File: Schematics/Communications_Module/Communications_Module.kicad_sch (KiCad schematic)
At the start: 72 parts, among them J1 USB_B_Micro, J2 SWD_01x04_Pin, J3 Stack Male Edge Connector, Q1 AO3400A, SW1 SW_STM_RESET, SW2 SW_STM_BOOT_MODE, U1 RFM95W-915S2, U2 W25Q128JVS, U3 AMS1117-3.3, U4 LM66100DCKR, U5 LM66100DCKR, U6 LM66100DCKR, U7 STM32F103CBT6, U8 ACS70331EOLC, U9 ISO1042BDWVR, Y1 X322516MMB4SI

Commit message: Power routed?
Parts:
- renumbered C6 to C5, C5 to C6, C2 to C7
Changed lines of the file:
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@@
     (title "QRET 23-24 SRAD Communications Module")
     (date "2024-03-09")
-    (rev "V0.3.0")
+    (rev "V0.3.1")
     (company "Queen's Rocket Engineering Team")
     (comment 1 "Contributors: Oak Campbell, Kennan Bays")
@@
   (symbol (lib_id "power:GND") (at 403.225 66.04 90) (unit 1)
     (in_bom yes) (on_board yes) (dnp no) (fields_autoplaced)
-    (property "Reference" "#PWR051" (at 409.575 66.04 0)
+    (property "Reference" "#PWR052" (at 409.575 66.04 0)
       (effects (font (size 1.27 1.27)) hide)
     )
@@
       (project "Communications_Module"
         (path "/ace06731-9b48-45c3-868d-c65fed1a8f9b"
-          (reference "#PWR051") (unit 1)
+          (reference "#PWR052") (unit 1)
         )
       )
@@
   (symbol (lib_id "power:GND") (at 403.86 46.99 0) (unit 1)
     (in_bom yes) (on_board yes) (dnp no)
-    (property "Reference" "#PWR053" (at 403.86 53.34 0)
+    (property "Reference" "#PWR054" (at 403.86 53.34 0)
       (effects (font (size 1.27 1.27)) hide)
     )
@@
       (project "Communications_Module"
         (path "/ace06731-9b48-45c3-868d-c65fed1a8f9b"
-          (reference "#PWR053") (unit 1)
+          (reference "#PWR054") (unit 1)
         )
       )
@@
   (symbol (lib_id "power:+3.3V") (at 403.86 31.75 0) (unit 1)
     (in_bom yes) (on_board yes) (dnp no)
-    (property "Reference" "#PWR052" (at 403.86 35.56 0)
+    (property "Reference" "#PWR053" (at 403.86 35.56 0)
       (effects (font (size 1.27 1.27)) hide)
     )
@@
       (project "Communications_Module"
         (path "/ace06731-9b48-45c3-868d-c65fed1a8f9b"
-          (reference "#PWR052") (unit 1)
+          (reference "#PWR053") (unit 1)
         )
       )
@@
   (symbol (lib_id "power:GND") (at 400.05 198.12 180) (unit 1)
     (in_bom yes) (on_board yes) (dnp no) (fields_autoplaced)
-    (property "Reference" "#PWR050" (at 400.05 191.77 0)
+    (property "Reference" "#PWR051" (at 400.05 191.77 0)
       (effects (font (size 1.27 1.27)) hide)
     )
@@
       (project "Communications_Module"
         (path "/ace06731-9b48-45c3-868d-c65fed1a8f9b"
-          (reference "#PWR050") (unit 1)
+          (reference "#PWR051") (unit 1)
         )
       )
@@
   (symbol (lib_id "Device:C") (at 92.71 253.365 0) (unit 1)
     (in_bom yes) (on_board yes) (dnp no)
-    (property "Reference" "C5" (at 86.36 252.095 0)
+    (property "Reference" "C6" (at 86.36 252.095 0)
       (effects (font (size 1.27 1.27)) (justify left))
     )
@@
       (project "Communications_Module"
         (path "/ace06731-9b48-45c3-868d-c65fed1a8f9b"
-          (reference "C5") (unit 1)
+          (reference "C6") (unit 1)
         )
       )
@@
   (symbol (lib_id "power:GND") (at 395.605 173.99 0) (unit 1)
     (in_bom yes) (on_board yes) (dnp no) (fields_autoplaced)
-    (property "Reference" "#PWR056" (at 395.605 180.34 0)
+    (property "Reference" "#PWR049" (at 395.605 180.34 0)
       (effects (font (size 1.27 1.27)) hide)
     )
@@
       (project "Communications_Module"
         (path "/ace06731-9b48-45c3-868d-c65fed1a8f9b"
-          (reference "#PWR056") (unit 1)
+          (reference "#PWR049") (unit 1)
         )
       )
@@
   (symbol (lib_id "Device:C_Polarized") (at 175.26 235.585 0) (unit 1)
     (in_bom yes) (on_board yes) (dnp no)
-    (property "Reference" "C2" (at 168.275 236.22 0)
+    (property "Reference" "C7" (at 168.275 236.22 0)
       (effects (font (size 1.27 1.27)) (justify left))
     )
@@
       (project "Communications_Module"
         (path "/ace06731-9b48-45c3-868d-c65fed1a8f9b"
-          (reference "C2") (unit 1)
+          (reference "C7") (unit 1)
         )
       )
@@
   (symbol (lib_id "power:+5V") (at 388.62 149.86 270) (unit 1)
     (in_bom yes) (on_board yes) (dnp no)
-    (property "Reference" "#PWR049" (at 384.81 149.86 0)
+    (property "Reference" "#PWR047" (at 384.81 149.86 0)
       (effects (font (size 1.27 1.27)) hide)
     )
@@
       (project "Communications_Module"
         (path "/ace06731-9b48-45c3-868d-c65fed1a8f9b"
-          (reference "#PWR049") (unit 1)
+          (reference "#PWR047") (unit 1)
         )
       )
@@
   (symbol (lib_id "power:GND") (at 397.51 220.98 0) (unit 1)
     (in_bom yes) (on_board yes) (dnp no) (fields_autoplaced)
-    (property "Reference" "#PWR047" (at 397.51 227.33 0)
+    (property "Reference" "#PWR050" (at 397.51 227.33 0)
       (effects (font (size 1.27 1.27)) hide)
     )
@@
       (project "Communications_Module"
         (path "/ace06731-9b48-45c3-868d-c65fed1a8f9b"
-          (reference "#PWR047") (unit 1)
+          (reference "#PWR050") (unit 1)
         )
       )
@@
   (symbol (lib_id "power:GND") (at 92.71 257.175 0) (unit 1)
     (in_bom yes) (on_board yes) (dnp no) (fields_autoplaced)
-    (property "Reference" "#PWR015" (at 92.71 263.525 0)
+    (property "Reference" "#PWR016" (at 92.71 263.525 0)
       (effects (font (size 1.27 1.27)) hide)
     )
@@
       (project "Communications_Module"
         (path "/ace06731-9b48-45c3-868d-c65fed1a8f9b"
-          (reference "#PWR015") (unit 1)
+          (reference "#PWR016") (unit 1)
         )
       )
@@
   (symbol (lib_id "power:GND") (at 92.71 238.125 0) (unit 1)
     (in_bom yes) (on_board yes) (dnp no) (fields_autoplaced)
-    (property "Reference" "#PWR016" (at 92.71 244.475 0)
+    (property "Reference" "#PWR015" (at 92.71 244.475 0)
       (effects (font (size 1.27 1.27)) hide)
     )
@@
       (project "Communications_Module"
         (path "/ace06731-9b48-45c3-868d-c65fed1a8f9b"
-          (reference "#PWR016") (unit 1)
+          (reference "#PWR015") (unit 1)
         )
       )
@@
   (symbol (lib_id "power:+5V") (at 408.94 205.74 270) (unit 1)
     (in_bom yes) (on_board yes) (dnp no)
-    (property "Reference" "#PWR054" (at 405.13 205.74 0)
+    (property "Reference" "#PWR055" (at 405.13 205.74 0)
       (effects (font (size 1.27 1.27)) hide)
     )
@@
       (project "Communications_Module"
         (path "/ace06731-9b48-45c3-868d-c65fed1a8f9b"
-          (reference "#PWR054") (unit 1)
+          (reference "#PWR055") (unit 1)
         )
       )
@@
   (symbol (lib_id "Device:C") (at 92.71 234.315 0) (unit 1)
     (in_bom yes) (on_board yes) (dnp no)
-    (property "Reference" "C6" (at 86.36 233.045 0)
+    (property "Reference" "C5" (at 86.36 233.045 0)
       (effects (font (size 1.27 1.27)) (justify left))
     )
@@
       (project "Communications_Module"
         (path "/ace06731-9b48-45c3-868d-c65fed1a8f9b"
-          (reference "C6") (unit 1)
+          (reference "C5") (unit 1)
         )
       )

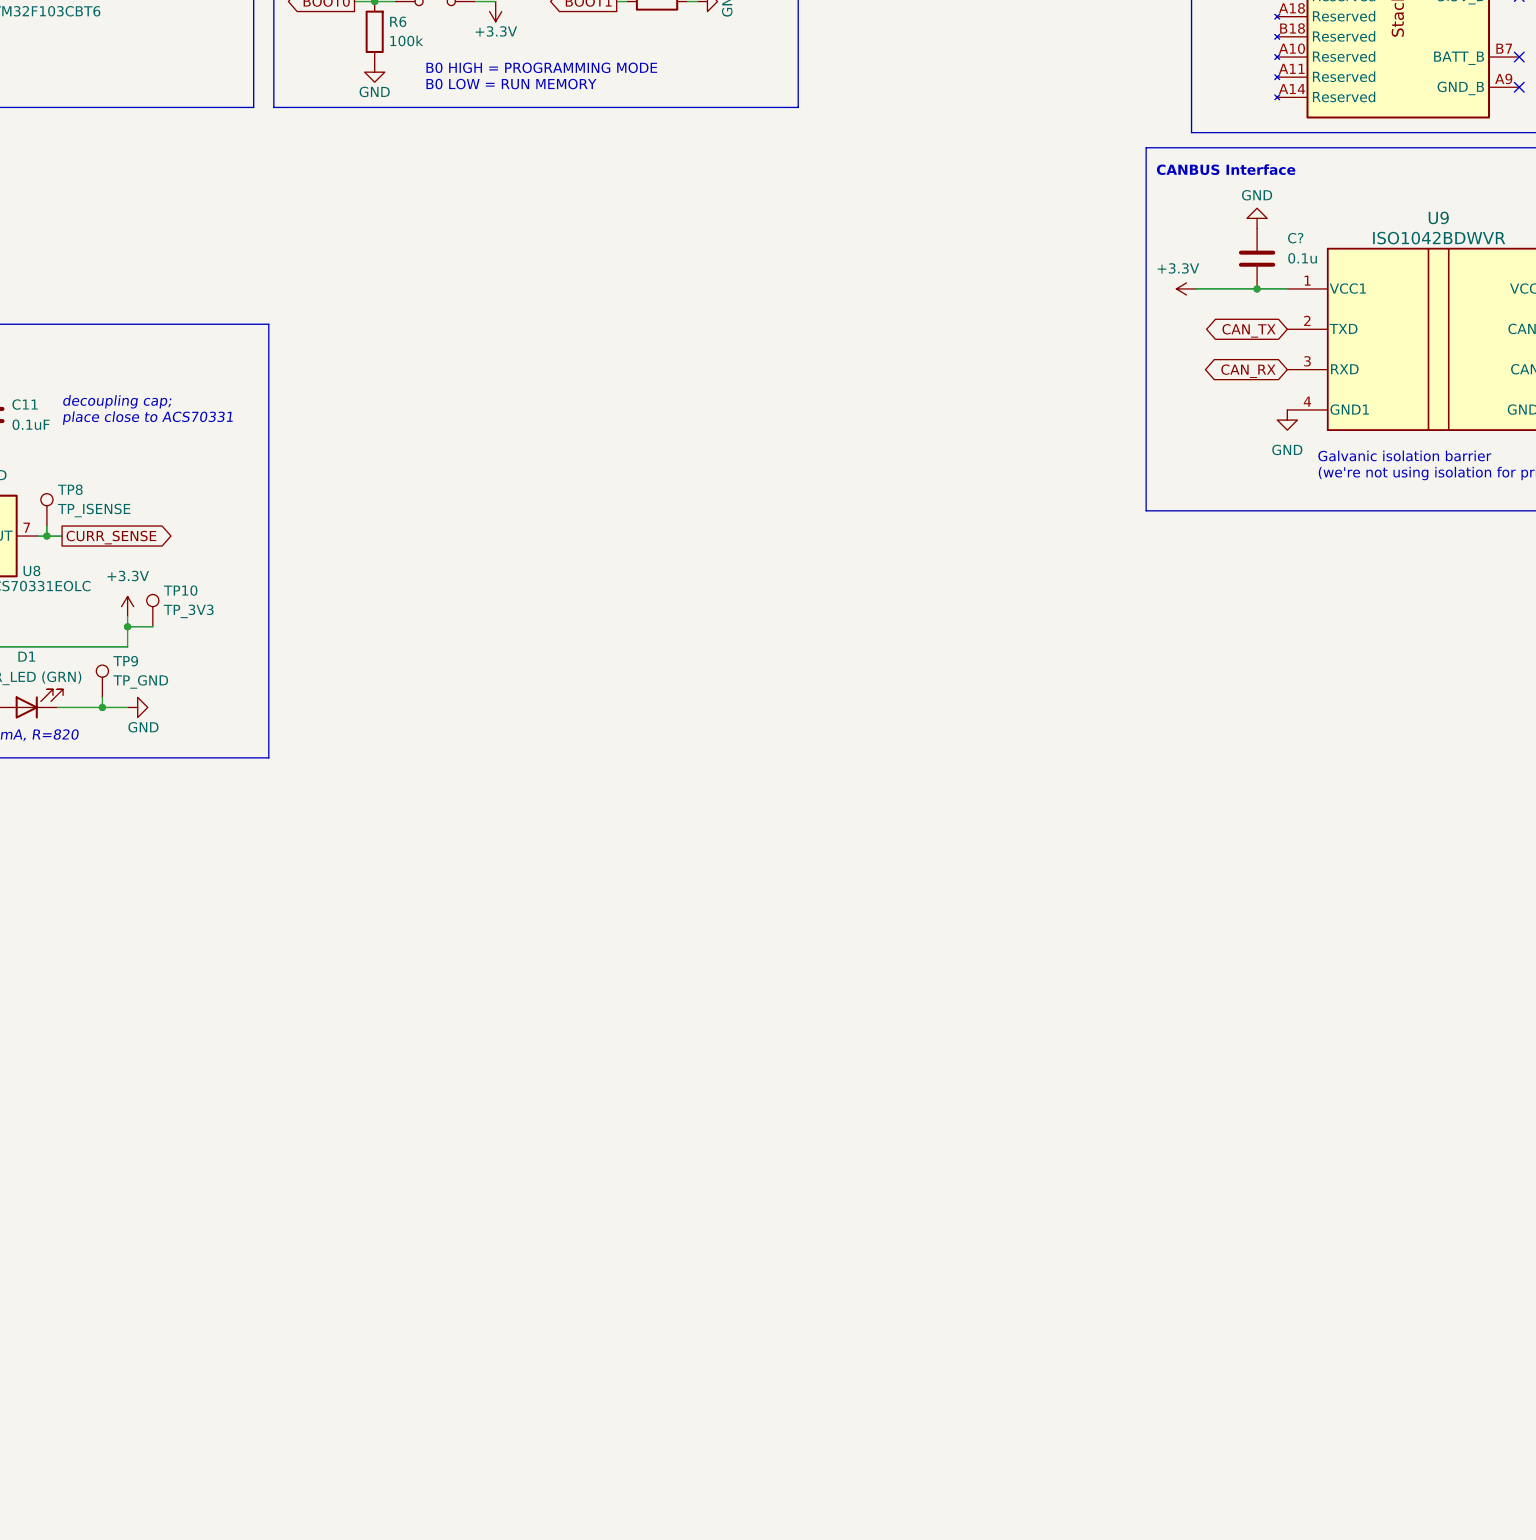
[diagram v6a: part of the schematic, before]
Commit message: Just a few tough traces left, no antenna yet. 'So close but so far'
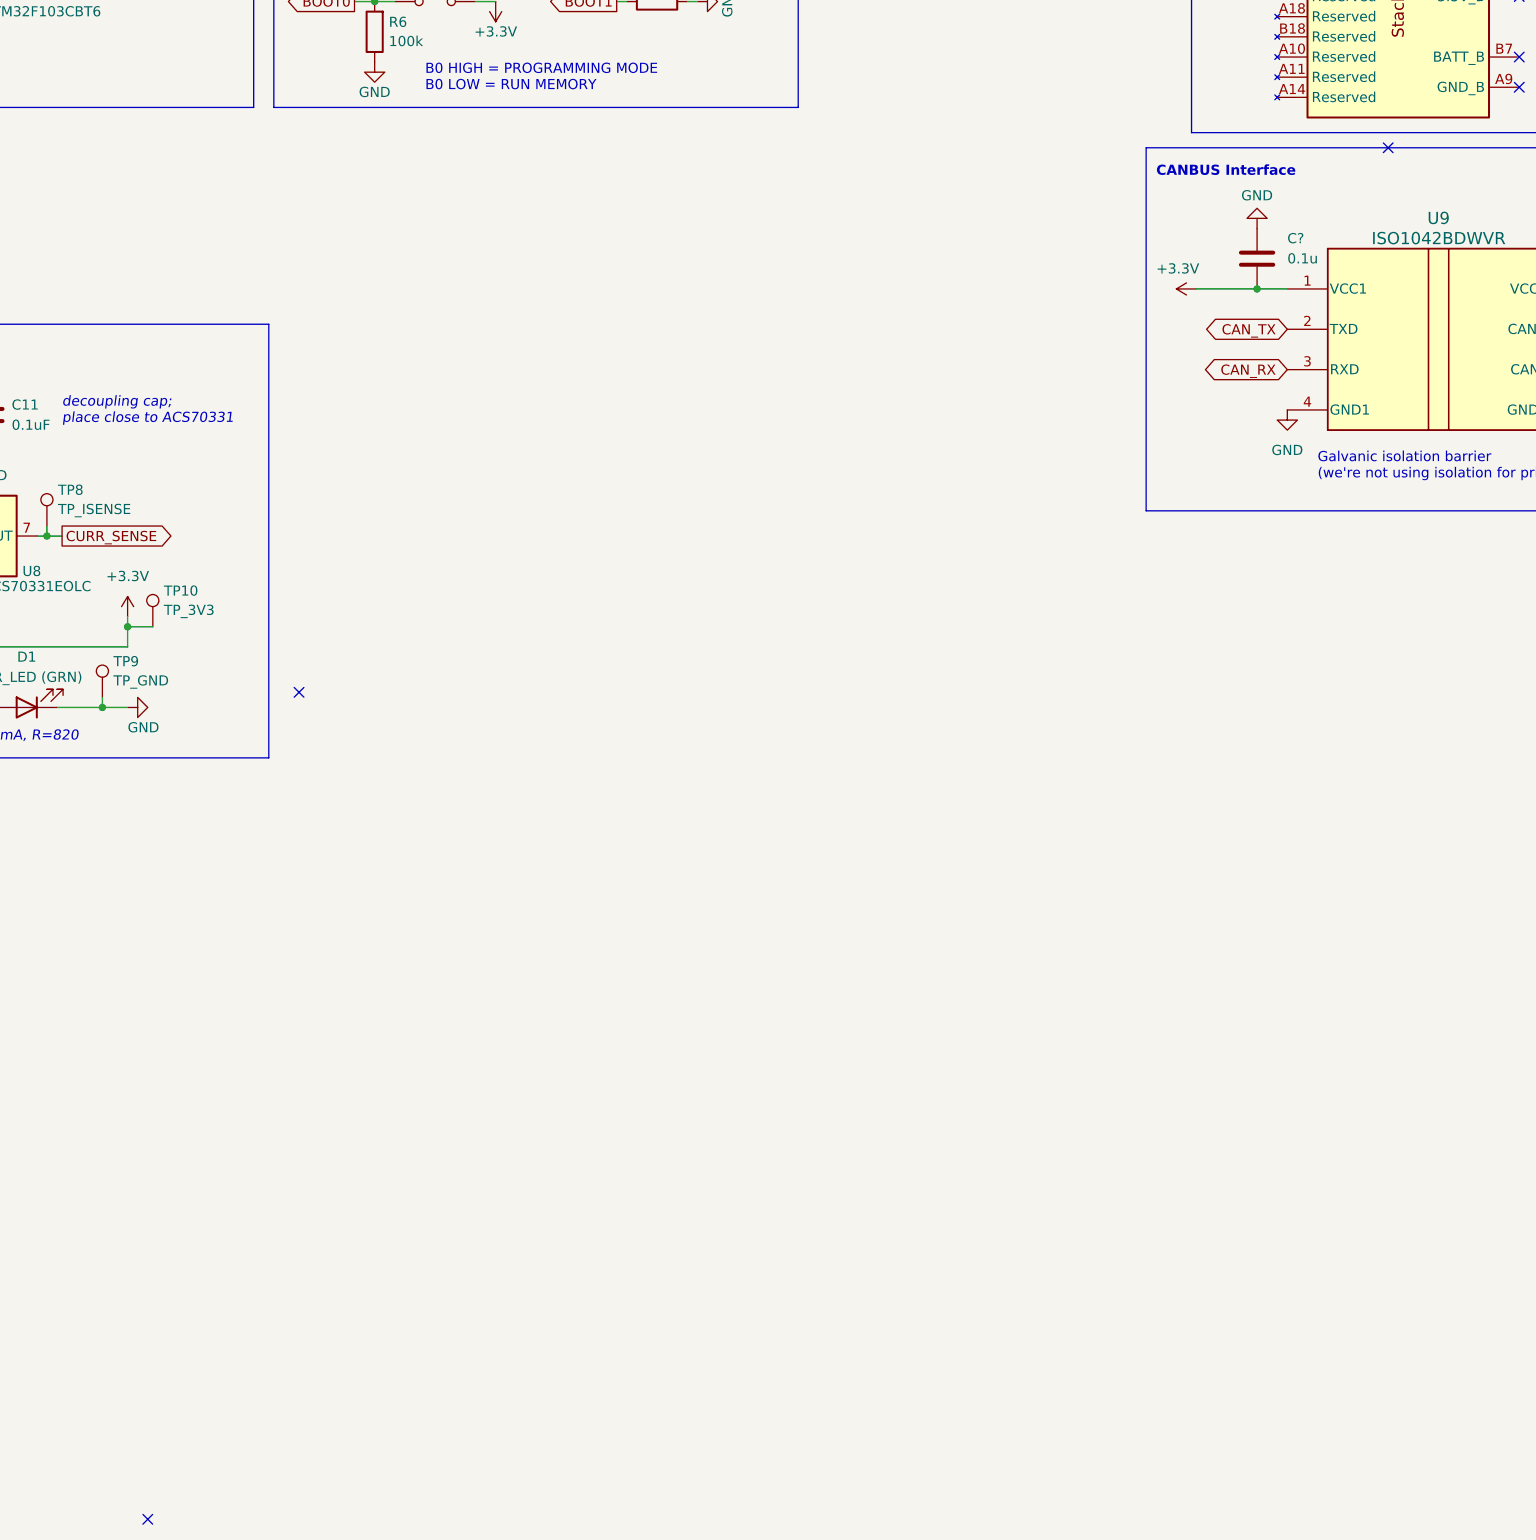
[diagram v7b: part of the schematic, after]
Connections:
- no-connect marks 16 -> 19
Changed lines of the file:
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@@
   (no_connect (at 388.62 180.34))
   (no_connect (at 175.26 151.13))
+  (no_connect (at 234.95 256.54))
   (no_connect (at 19.05 253.365))
   (no_connect (at 175.26 133.35))
@@
   (no_connect (at 66.04 40.64))
   (no_connect (at 66.04 38.1))
+  (no_connect (at 215.9 360.68))
   (no_connect (at 411.48 39.37))
   (no_connect (at 66.04 35.56))
   (no_connect (at 175.26 115.57))
+  (no_connect (at 372.11 187.96))
   (wire (pts (xy 181.61 217.805) (xy 191.77 217.805))
     (stroke (width 0) (type default))

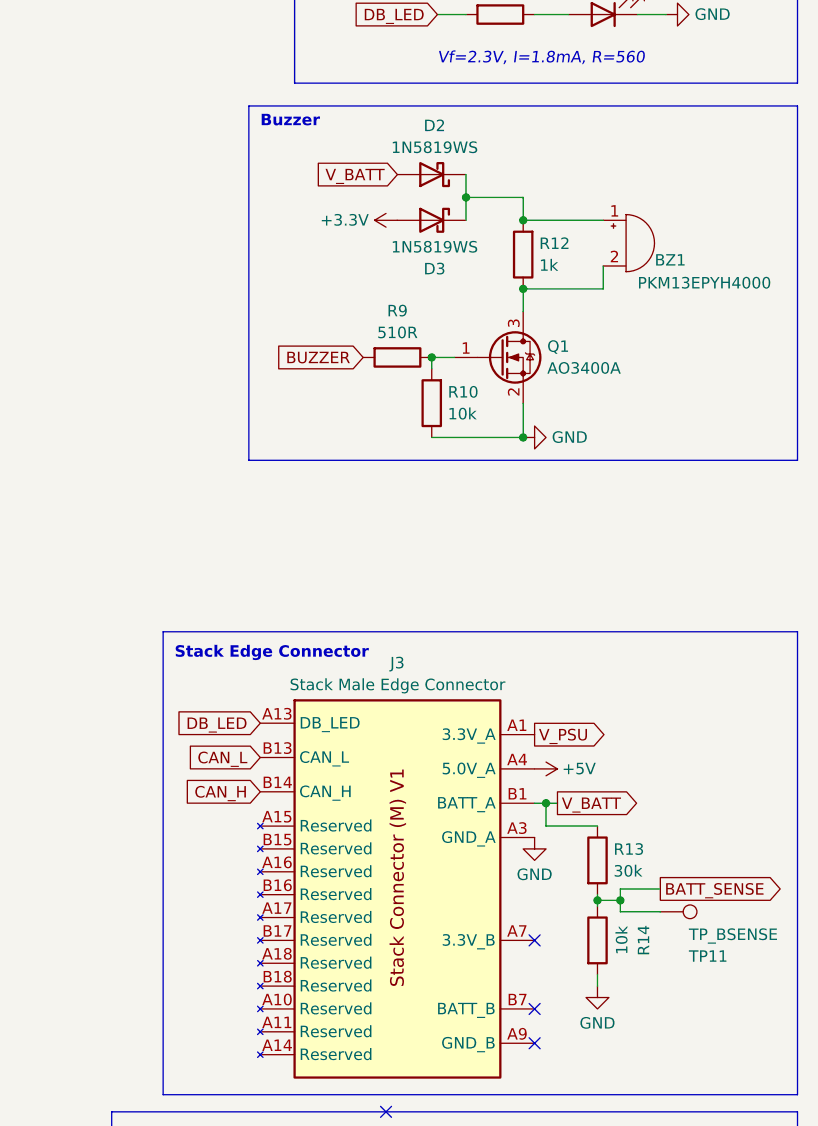
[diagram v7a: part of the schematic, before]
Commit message: Small hardware tweaks (PCB update required)
-Changed bootmode/reset switches from PTS636 to TS1187
-Fixed buzzer gate driver
-Disconnected debug LED from edge connector
-Updated capacitor footprints for analog filtering
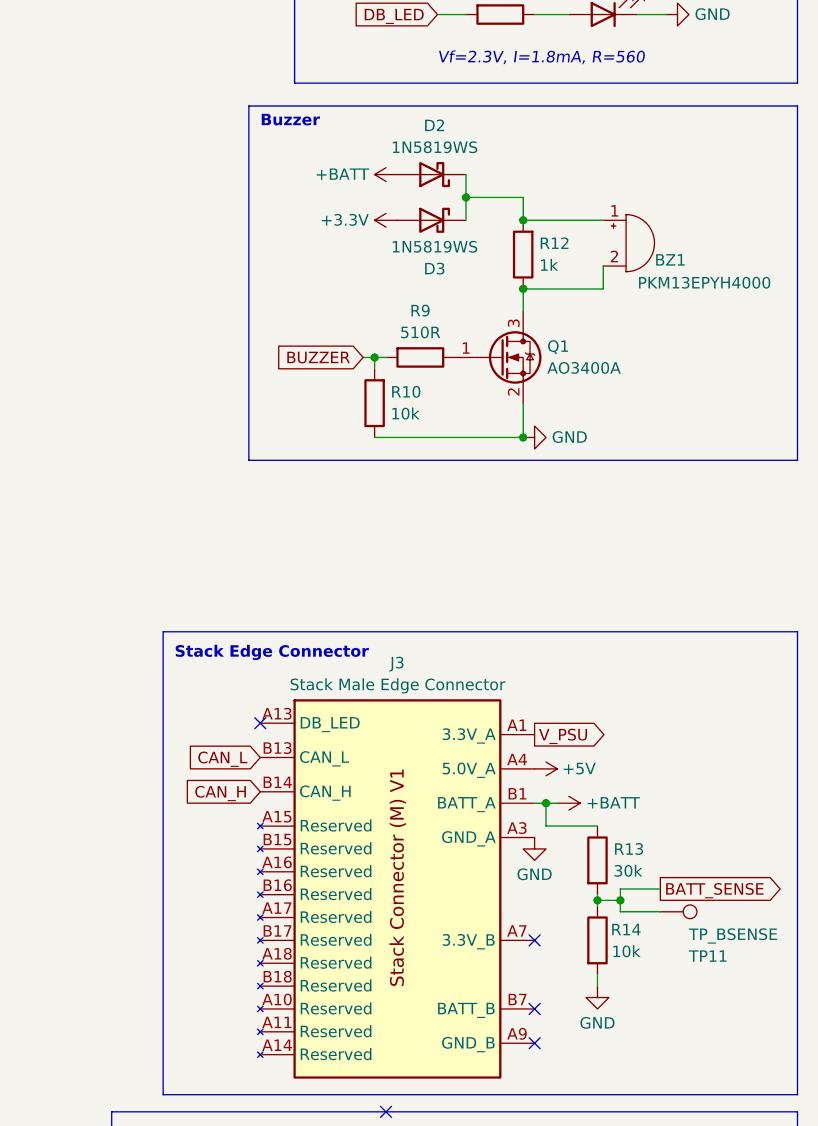
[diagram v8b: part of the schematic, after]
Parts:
- C17, C19: footprint Capacitor_SMD:CP_Elec_4x5.4 -> Capacitor_SMD:C_0805_2012Metric; Digikey 732-8541-1-ND -> (none); LCSC (none) -> C28323
- SW1, SW2: footprint PTS636:PTS636_SK43_SMTR_LFS -> Button_Switch_SMD:SW_Push_1P1T_XKB_TS-1187A; Digikey PTS636 SK43 SMTR LFS -> (none); LCSC (none) -> C318884
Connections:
- net BUZZER: now also R10.2
- net DB_LED: no longer J3.A13 (DB_LED)
- net at Q1.1 (G), R9.1: no longer R10.2
- net V_BATT renamed +BATT
- no-connect marks 19 -> 20
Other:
- moved on the sheet: R10, R9
